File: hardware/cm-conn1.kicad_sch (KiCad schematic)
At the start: 0 parts

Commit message: CM4 connectors: add symbols/footprints, connect power pins
- Copy CM4 symbol and footprint from pedalboard-hw to granit library
- Remove all pedalboard library references
- Connect GND and +5V power pins on both connectors
- PSU GND ERC error resolved
- 0 ERC warnings, remaining errors are expected unconnected signal pins
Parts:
- added CM1: CM4, granit:Raspberry-Pi-4-Compute-Module, symbol granit:CM4
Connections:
- new net +5VP: CM1.77 (+5v_(Input)), CM1.79 (+5v_(Input)), CM1.81 (+5v_(Input)), CM1.83 (+5v_(Input)), CM1.85 (+5v_(Input)), CM1.87 (+5v_(Input))
- new net GND: CM1.1 (GND), CM1.13 (GND), CM1.14 (GND), CM1.2 (GND), CM1.22 (GND), CM1.23 (GND), CM1.32 (GND), CM1.33 (GND), CM1.42 (GND), CM1.43 (GND), CM1.52 (GND), CM1.53 (GND), CM1.59 (GND), CM1.60 (GND), CM1.65 (GND), CM1.66 (GND), CM1.7 (GND), CM1.71 (GND), CM1.74 (GND), CM1.8 (GND), CM1.98 (GND)

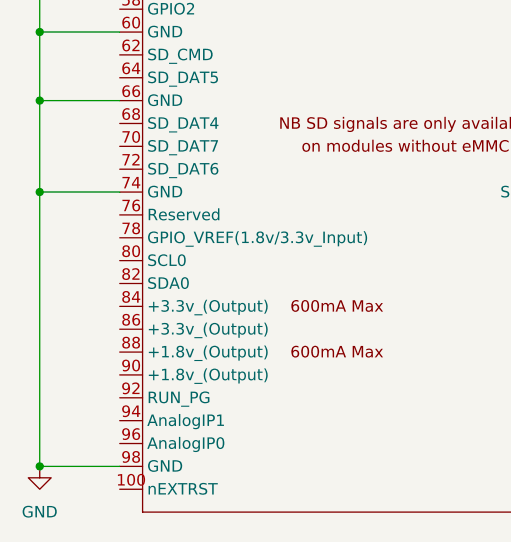
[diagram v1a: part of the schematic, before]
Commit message: CI: use KiBot dev branch with KiCad 10 support
KiBot 1.8.6 (dev) can parse KiCad 10 files.
Install from git dev branch + KiCad 10 PPA on ubuntu-latest.
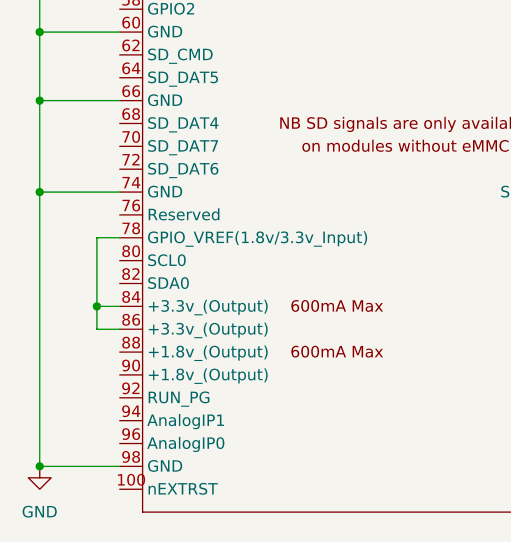
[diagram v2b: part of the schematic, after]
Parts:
- CM1: footprint granit:Raspberry-Pi-4-Compute-Module -> Pedalboard Library:Raspberry-Pi-4-Compute-Module; symbol granit:CM4 -> pedalboard:CM4
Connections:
- net at CM1.78 (GPIO_VREF(1.8v/3.3v_Input)): now also CM1.84 (+3.3v_(Output)), CM1.86 (+3.3v_(Output))
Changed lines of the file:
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@@
 		(color 0 0 0 0)
 	)
+	(junction
+		(at 52.07 144.78)
+		(diameter 0)
+		(color 0 0 0 0)
+	)
 	(wire
 		(pts
@@
 	(wire
 		(pts
+			(xy 54.61 137.16) (xy 52.07 137.16)
+		)
+		(stroke
+			(width 0)
+			(type default)
+		)
+	)
+	(wire
+		(pts
 			(xy 45.72 104.14) (xy 45.72 114.3)
 		)
@@
 	(wire
 		(pts
+			(xy 54.61 147.32) (xy 52.07 147.32)
+		)
+		(stroke
+			(width 0)
+			(type default)
+		)
+	)
+	(wire
+		(pts
 			(xy 115.57 144.78) (xy 121.92 144.78)
 		)
@@
 	(wire
 		(pts
+			(xy 52.07 147.32) (xy 52.07 144.78)
+		)
+		(stroke
+			(width 0)
+			(type default)
+		)
+	)
+	(wire
+		(pts
 			(xy 121.92 40.64) (xy 121.92 48.26)
 		)
@@
 	(wire
 		(pts
+			(xy 52.07 144.78) (xy 54.61 144.78)
+		)
+		(stroke
+			(width 0)
+			(type default)
+		)
+	)
+	(wire
+		(pts
 			(xy 45.72 78.74) (xy 45.72 91.44)
 		)
@@
 		(pts
 			(xy 115.57 81.28) (xy 121.92 81.28)
+		)
+		(stroke
+			(width 0)
+			(type default)
+		)
+	)
+	(wire
+		(pts
+			(xy 52.07 137.16) (xy 52.07 144.78)
 		)
 		(stroke
@@
 	)
 	(symbol
-		(lib_id "granit:CM4")
+		(lib_id "pedalboard:CM4")
 		(at 87.63 96.52 0)
 		(unit 1)
@@
 			)
 		)
-		(property "Footprint" "granit:Raspberry-Pi-4-Compute-Module"
+		(property "Footprint" "Pedalboard Library:Raspberry-Pi-4-Compute-Module"
 			(at 229.87 123.19 0)
 			(hide yes)
